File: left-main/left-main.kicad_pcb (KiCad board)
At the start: 2 copper layers, 136 x 123.8 mm, 205 parts, among them P1 CONN_4, P2 CONN_5, P3 CONN_6, P4 CONN_18, Q1 PNP, Q2 PNP, SW11 SPST, SW12 SPST, SW13 SPST, SW14 SPST, SW15 SPST, SW16 SPST, SW17 SPST, SW21 SPST, SW22 SPST, SW23 SPST, SW24 SPST, SW25 SPST, SW27 SPST, SW31 SPST, SW32 SPST, SW33 SPST, SW34 SPST, SW35 SPST, SW37 SPST, SW411 SPST, SW412 SPST, SW42 SPST, SW43 SPST, SW44 SPST, SW45 SPST, SW46 SPST, SW47 SPST, SW51 SPST, SW52 SPST, SW53 SPST, SW54 SPST, SW55 SPST, SW56 SPST, U1 ATMEGA88-A, U2 PCA9634, U3 TPIC6C595, X1 16Mhz

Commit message: Switch 15
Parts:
- SW15: footprint UGL:Cherry_MX -> ugl:Cherry-MX-Matias-Hybrid
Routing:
- net /KEYS_ROW1: track 165.8 -> 166.5 mm
- net Net-(D15-Pad2): track 18.7 -> 17.9 mm
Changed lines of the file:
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@@
 (kicad_pcb (version 4) (host pcbnew 4.0.1-stable)
   (general
-    (links 366)
+    (links 368)
     (no_connects 0)
-    (area 29.35 17.5462 270.000001 165.000001)
+    (area 125.815009 33.896633 261.825015 157.725219)
     (thickness 1.6)
     (drawings 431)
-    (tracks 1379)
+    (tracks 1386)
     (zones 0)
     (modules 205)
@@
   (layers
     (0 F.Cu signal)
-    (31 B.Cu signal)
+    (31 B.Cu signal hide)
     (32 B.Adhes user hide)
     (33 F.Adhes user hide)
@@
   )
   (module UGL:Cherry_MX locked (layer F.Cu)
-    (at 212.820002 65.320214 180)
-    (fp_text reference SW15 (at 0 4.9 180) (layer F.SilkS)
-      (effects (font (size 1.5 1.5) (thickness 0.3)))
-    )
-    (fp_text value SPST (at 0 0 180) (layer F.SilkS) hide
-      (effects (font (size 1.5 1.5) (thickness 0.3)))
-    )
-    (fp_line (start -7.6 -7.6) (end -7.6 7.6) (layer B.SilkS) (width 0.15))
-    (fp_line (start -7.6 7.6) (end 7.6 7.6) (layer B.SilkS) (width 0.15))
-    (fp_line (start 7.6 -7.6) (end 7.6 7.6) (layer B.SilkS) (width 0.15))
-    (fp_line (start -7.6 -7.6) (end 7.6 -7.6) (layer B.SilkS) (width 0.15))
-    (fp_line (start -7.62 -7.62) (end 7.62 -7.62) (layer F.SilkS) (width 0.15))
-    (fp_line (start 7.62 -7.62) (end 7.62 7.62) (layer F.SilkS) (width 0.15))
-    (fp_line (start 7.62 7.62) (end -7.62 7.62) (layer F.SilkS) (width 0.15))
-    (fp_line (start -7.62 7.62) (end -7.62 -7.62) (layer F.SilkS) (width 0.15))
-    (pad "" np_thru_hole circle (at 0 0 180) (size 4 4) (drill 4) (layers *.Cu *.Mask F.SilkS))
-    (pad 2 thru_hole circle (at -3.81 -2.54 180) (size 2.5 2.5) (drill 1.5) (layers *.Cu *.Mask F.SilkS)
-      (net 54 "Net-(D15-Pad2)"))
-    (pad 1 thru_hole circle (at 2.54 -5.08 180) (size 2.5 2.5) (drill 1.5) (layers *.Cu *.Mask F.SilkS)
-      (net 9 /KEYS_ROW1))
-  )
-  (module UGL:Cherry_MX locked (layer F.Cu)
     (at 143.57001 103.320221 180)
     (fp_text reference SW31 (at 0 4.9 180) (layer F.SilkS)
@@
     )
   )
+  (module ugl:Cherry-MX-Matias-Hybrid locked (layer F.Cu)
+    (at 212.820002 65.320214 180)
+    (tags switch)
+    (fp_text reference SW15 (at 0 3.81 180) (layer F.SilkS)
+      (effects (font (thickness 0.3048)))
+    )
+    (fp_text value SPST (at 0 0 180) (layer F.SilkS) hide
+      (effects (font (thickness 0.3048)))
+    )
+    (fp_line (start -7.62 7.62) (end -7.62 -7.62) (layer B.SilkS) (width 0.15))
+    (fp_line (start 7.62 7.62) (end -7.62 7.62) (layer B.SilkS) (width 0.15))
+    (fp_line (start 7.62 -7.62) (end 7.62 7.62) (layer B.SilkS) (width 0.15))
+    (fp_line (start -7.62 -7.62) (end 7.62 -7.62) (layer B.SilkS) (width 0.15))
+    (fp_line (start -7.75 -6.4) (end -7.75 6.4) (layer F.SilkS) (width 0.15))
+    (fp_line (start 7.75 -6.4) (end 7.75 6.4) (layer F.SilkS) (width 0.15))
+    (fp_line (start -7.75 6.4) (end 7.75 6.4) (layer F.SilkS) (width 0.15))
+    (fp_line (start -7.75 -6.4) (end 7.75 -6.4) (layer F.SilkS) (width 0.15))
+    (fp_line (start -7.62 -7.62) (end 7.62 -7.62) (layer F.SilkS) (width 0.15))
+    (fp_line (start 7.62 -7.62) (end 7.62 7.62) (layer F.SilkS) (width 0.15))
+    (fp_line (start 7.62 7.62) (end -7.62 7.62) (layer F.SilkS) (width 0.15))
+    (fp_line (start -7.62 7.62) (end -7.62 -7.62) (layer F.SilkS) (width 0.15))
+    (pad 0 thru_hole circle (at 0 0 180) (size 3.98018 3.98018) (drill 3.98018) (layers *.Cu *.Mask F.SilkS))
+    (pad 1 thru_hole circle (at 2.54 -5.08 180) (size 2.6 2.6) (drill 1.5011) (layers *.Cu *.Mask F.SilkS)
+      (net 9 /KEYS_ROW1))
+    (pad 2 thru_hole circle (at -3.81 -2.54 180) (size 2.6 2.6) (drill 1.5011) (layers *.Cu *.Mask F.SilkS)
+      (net 54 "Net-(D15-Pad2)"))
+    (pad "" thru_hole circle (at -5.08 0 180) (size 1.69926 1.69926) (drill 1.69926) (layers *.Cu *.Mask F.SilkS))
+    (pad "" thru_hole circle (at 5.08 0 180) (size 1.69926 1.69926) (drill 1.69926) (layers *.Cu *.Mask F.SilkS))
+    (pad 1 thru_hole circle (at 2.5 -4.5 180) (size 2.5 2.5) (drill 1.5) (layers *.Cu *.Mask F.SilkS)
+      (net 9 /KEYS_ROW1))
+    (pad 2 thru_hole circle (at -2.5 -4 180) (size 2.5 2.5) (drill 1.5) (layers *.Cu *.Mask F.SilkS)
+      (net 54 "Net-(D15-Pad2)"))
+    (model cherry_mx1.wrl
+      (at (xyz 0 0 0))
+      (scale (xyz 1 1 1))
+      (rotate (xyz 0 0 0))
+    )
+  )
   (gr_line (start 173.482 68.707) (end 170.561 68.707) (angle 90) (layer B.SilkS) (width 0.2))
   (gr_line (start 158.369 69.723) (end 161.036 69.723) (angle 90) (layer B.SilkS) (width 0.2))
@@
   (segment (start 238.5563 60.896) (end 241.3 63.6397) (width 0.4064) (layer B.Cu) (net 8))
   (segment (start 233.3937 112.796) (end 231.6937 114.496) (width 0.4064) (layer B.Cu) (net 8))
+  (segment (start 229.320002 69.820214) (end 230.570001 71.070213) (width 0.4064) (layer F.Cu) (net 9))
+  (segment (start 230.570001 71.070213) (end 245.771526 71.070213) (width 0.4064) (layer F.Cu) (net 9))
+  (segment (start 245.771526 71.070213) (end 246.441525 70.400214) (width 0.4064) (layer F.Cu) (net 9))
+  (segment (start 246.441525 70.400214) (end 248.280002 70.400214) (width 0.4064) (layer F.Cu) (net 9))
+  (segment (start 210.280002 70.400214) (end 211.580001 71.700213) (width 0.4064) (layer F.Cu) (net 9))
+  (segment (start 211.580001 71.700213) (end 227.980003 71.700213) (width 0.4064) (layer F.Cu) (net 9))
+  (segment (start 227.980003 71.700213) (end 229.280002 70.400214) (width 0.4064) (layer F.Cu) (net 9))
   (segment (start 210.280002 70.400214) (end 208.512236 70.400214) (width 0.4064) (layer F.Cu) (net 9))
   (segment (start 208.512236 70.400214) (end 207.212237 71.700213) (width 0.4064) (layer F.Cu) (net 9))
@@
   (segment (start 188.935835 70.976615) (end 189.512236 70.400214) (width 0.4064) (layer F.Cu) (net 9))
   (segment (start 189.512236 70.400214) (end 191.280002 70.400214) (width 0.4064) (layer F.Cu) (net 9))
-  (segment (start 229.320002 69.820214) (end 230.570001 71.070213) (width 0.4064) (layer F.Cu) (net 9))
-  (segment (start 247.070003 71.070213) (end 248.320002 69.820214) (width 0.4064) (layer F.Cu) (net 9))
-  (segment (start 230.570001 71.070213) (end 247.070003 71.070213) (width 0.4064) (layer F.Cu) (net 9))
   (segment (start 153.32001 69.820214) (end 155.087776 69.820214) (width 0.4064) (layer F.Cu) (net 9))
   (segment (start 155.087776 69.820214) (end 156.244177 70.976615) (width 0.4064) (layer F.Cu) (net 9))
@@
   (segment (start 148.657 109.5766) (end 148.757 109.6766) (width 0.4064) (layer B.Cu) (net 9))
   (segment (start 153.207 70.473224) (end 153.28001 70.400214) (width 0.4064) (layer B.Cu) (net 9))
-  (segment (start 229.280002 70.400214) (end 210.280002 70.400214) (width 0.4064) (layer F.Cu) (net 9))
   (segment (start 137.357 73.477204) (end 134.28001 70.400214) (width 0.4064) (layer B.Cu) (net 9))
   (segment (start 137.357 74.796) (end 137.357 73.477204) (width 0.4064) (layer B.Cu) (net 9))
@@
   (segment (start 154.657 110.096) (end 154.657 129.54086) (width 0.4064) (layer F.Cu) (net 39))
   (segment (start 154.657 129.54086) (end 156.912141 131.796001) (width 0.4064) (layer F.Cu) (net 39))
+  (segment (start 212.307 59.346) (end 211.855289 59.346) (width 0.4064) (layer B.Cu) (net 40))
+  (segment (start 206.357 66.213501) (end 206.357 66.896) (width 0.4064) (layer B.Cu) (net 40))
+  (segment (start 211.855289 59.346) (end 206.357 64.844289) (width 0.4064) (layer B.Cu) (net 40))
+  (segment (start 206.357 64.844289) (end 206.357 66.213501) (width 0.4064) (layer B.Cu) (net 40))
+  (segment (start 212.307 54.296) (end 212.307 59.346) (width 0.4064) (layer B.Cu) (net 40))
   (segment (start 194.367454 61.225954) (end 196.664669 61.225954) (width 0.4064) (layer B.Cu) (net 40))
   (segment (start 191.423511 64.169897) (end 194.367454 61.225954) (width 0.4064) (layer B.Cu) (net 40))
@@
   (segment (start 235.770459 142.65708) (end 237.886015 144.772636) (width 0.4064) (layer B.Cu) (net 40))
   (segment (start 237.886015 145.037704) (end 240.07893 147.230619) (width 0.4064) (layer B.Cu) (net 40))
-  (segment (start 212.307 54.296) (end 212.307 60.946) (width 0.4064) (layer B.Cu) (net 40))
   (via (at 206.357 66.896) (size 0.9652) (drill 0.5588) (layers F.Cu B.Cu) (net 40))
   (segment (start 206.357 66.896) (end 203.957 66.896) (width 0.4064) (layer F.Cu) (net 40))
   (via (at 203.957 66.896) (size 0.9652) (drill 0.5588) (layers F.Cu B.Cu) (net 40))
-  (segment (start 212.307 60.946) (end 206.357 66.896) (width 0.4064) (layer B.Cu) (net 40))
   (segment (start 162.397347 98.831437) (end 173.349035 98.831437) (width 0.4064) (layer B.Cu) (net 40))
   (segment (start 173.349035 98.831437) (end 178.587395 93.593077) (width 0.4064) (layer B.Cu) (net 40))
@@
   (segment (start 197.630002 68.859698) (end 191.6937 74.796) (width 0.4064) (layer B.Cu) (net 53))
   (segment (start 197.630002 67.860214) (end 197.630002 68.859698) (width 0.4064) (layer B.Cu) (net 53))
-  (segment (start 201.5937 73.4593) (end 201.5937 74.796) (width 0.4064) (layer B.Cu) (net 54))
-  (segment (start 206.557 68.496) (end 201.5937 73.4593) (width 0.4064) (layer B.Cu) (net 54))
-  (segment (start 215.994216 68.496) (end 206.557 68.496) (width 0.4064) (layer B.Cu) (net 54))
+  (segment (start 201.5937 74.796) (end 202.5823 74.796) (width 0.4064) (layer B.Cu) (net 54))
+  (segment (start 214.070003 68.070215) (end 215.320002 69.320214) (width 0.4064) (layer B.Cu) (net 54))
+  (segment (start 202.5823 74.796) (end 209.308085 68.070215) (width 0.4064) (layer B.Cu) (net 54))
+  (segment (start 209.308085 68.070215) (end 214.070003 68.070215) (width 0.4064) (layer B.Cu) (net 54))
   (segment (start 216.630002 67.860214) (end 215.994216 68.496) (width 0.4064) (layer B.Cu) (net 54))
   (segment (start 235.630002 67.860214) (end 235.630002 68.010214) (width 0.4064) (layer B.Cu) (net 55))

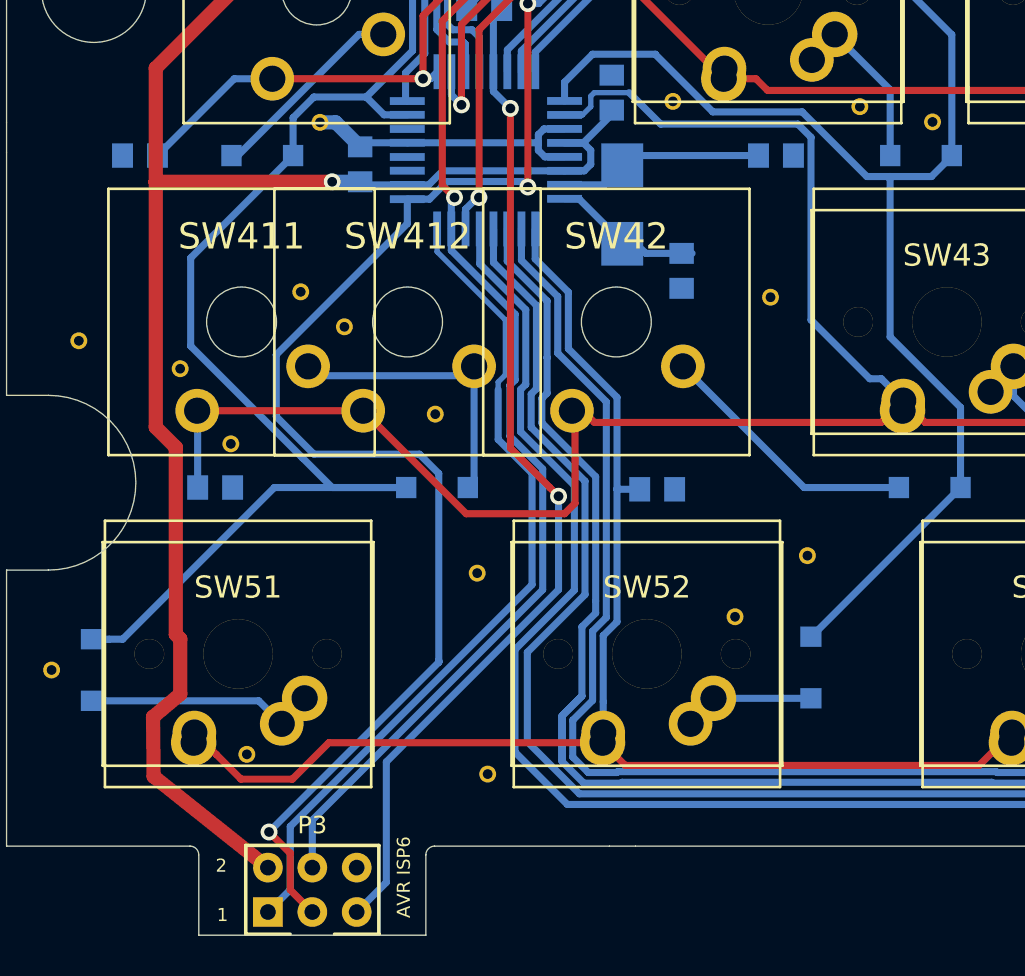
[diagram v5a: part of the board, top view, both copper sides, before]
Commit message: Changes iso keys to matias / cherry mx with holes
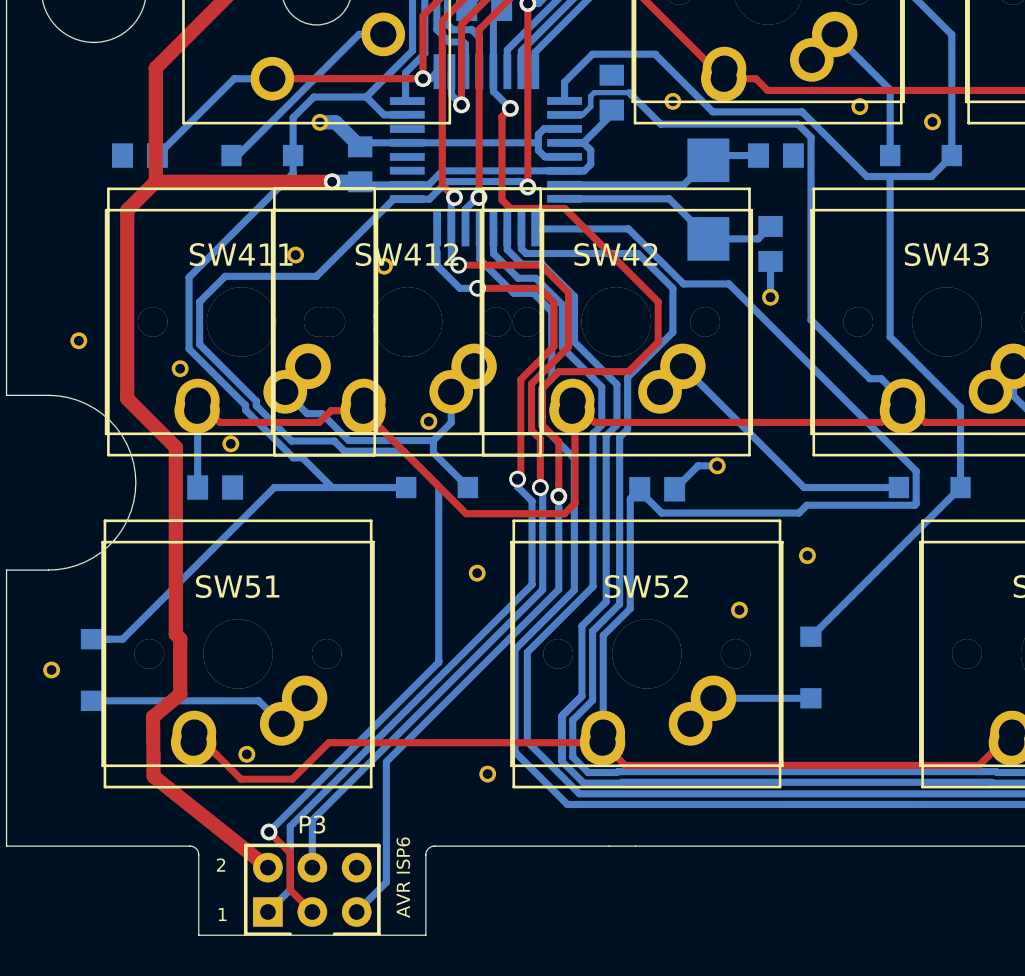
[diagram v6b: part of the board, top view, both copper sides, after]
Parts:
- added via 38/22mil: VAL**, ugl:via_38_22mil, F.Cu at (166.5, 130.6)
- SW411, SW412: footprint UGL:Cherry_MX -> ugl:Cherry-MX-Matias-Hybrid
- SW42: footprint ugl:Cherry_MX -> ugl:Cherry-MX-Matias-Hybrid
- moved C2 5.32 mm to (169.5, 117.9)
- moved X1 4.94 mm to (166.0, 115.3)
- moved via 35/25mil 4.16 mm to (147.4, 119.1)
- moved via 38/22mil 2.12 mm to (142.4, 118.5)
- moved via 35/25mil 0.56 mm to (150.0, 128.0)
- moved via 38/22mil 0.46 mm to (167.8, 138.8)
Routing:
- net /KEYS_ROW5: track 157.3 -> 185.6 mm
- net /RESET: track 58.2 -> 68.3 mm
- net /SCK: track 150.3 -> 157.2 mm
- net /KEYS_COL3: track 160.0 -> 166.9 mm
- net /XTAL2: track 7.47 -> 13.9 mm
- net Net-(D41-Pad2): track 17.0 -> 22.4 mm
- net GND: track 79.1 -> 84.2 mm
- net /MOSI: track 135.5 -> 139.8 mm, vias 2 -> 4
- net /MISO: track 48.1 -> 52.2 mm, vias 0 -> 2
- net Net-(D42-Pad2): track 15.4 -> 17.2 mm
- net /KEYS_COL4: track 205.4 -> 206.9 mm
- net VCC: track 394.0 -> 395.4 mm
- net /RX2: track 135.2 -> 136.4 mm
- net /KEYS_COL5: track 270.0 -> 270.9 mm
- net /KEYS_ROW4: track 168.6 -> 169.4 mm

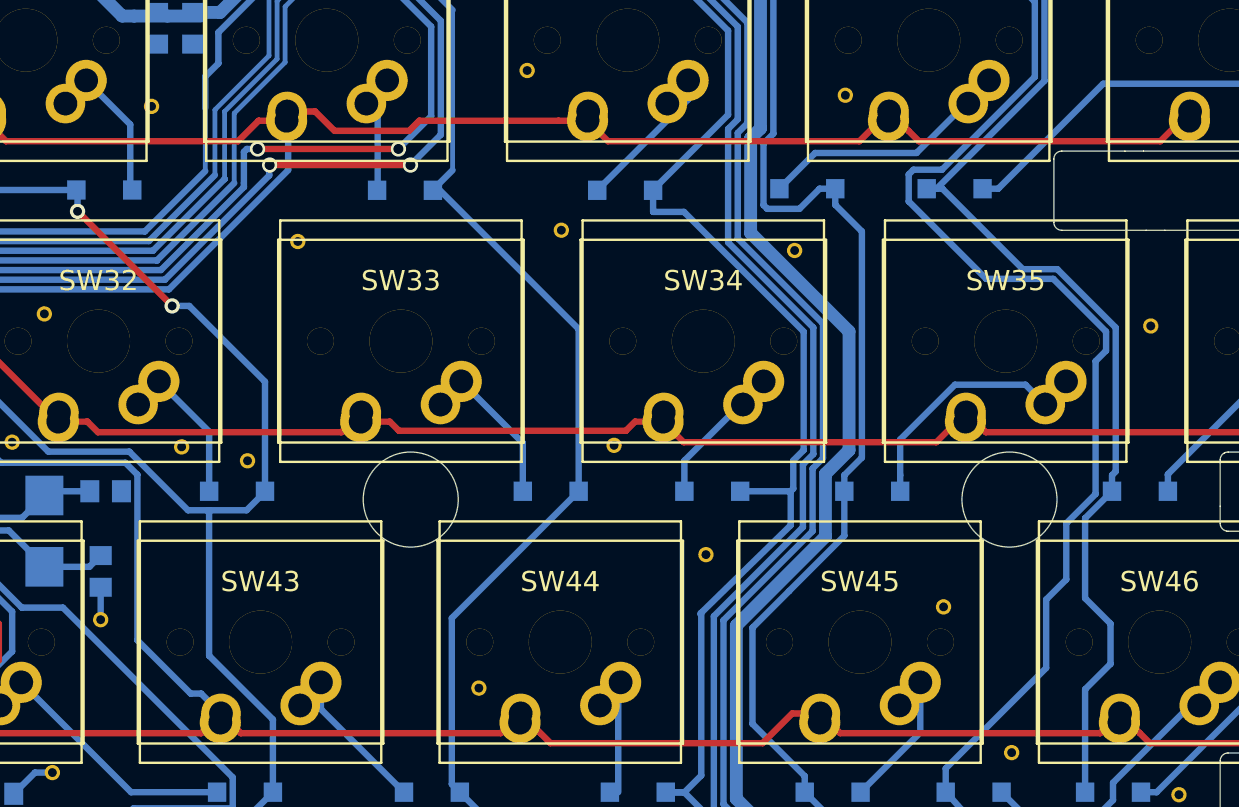
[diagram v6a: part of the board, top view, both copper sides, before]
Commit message: Adds more fill holes
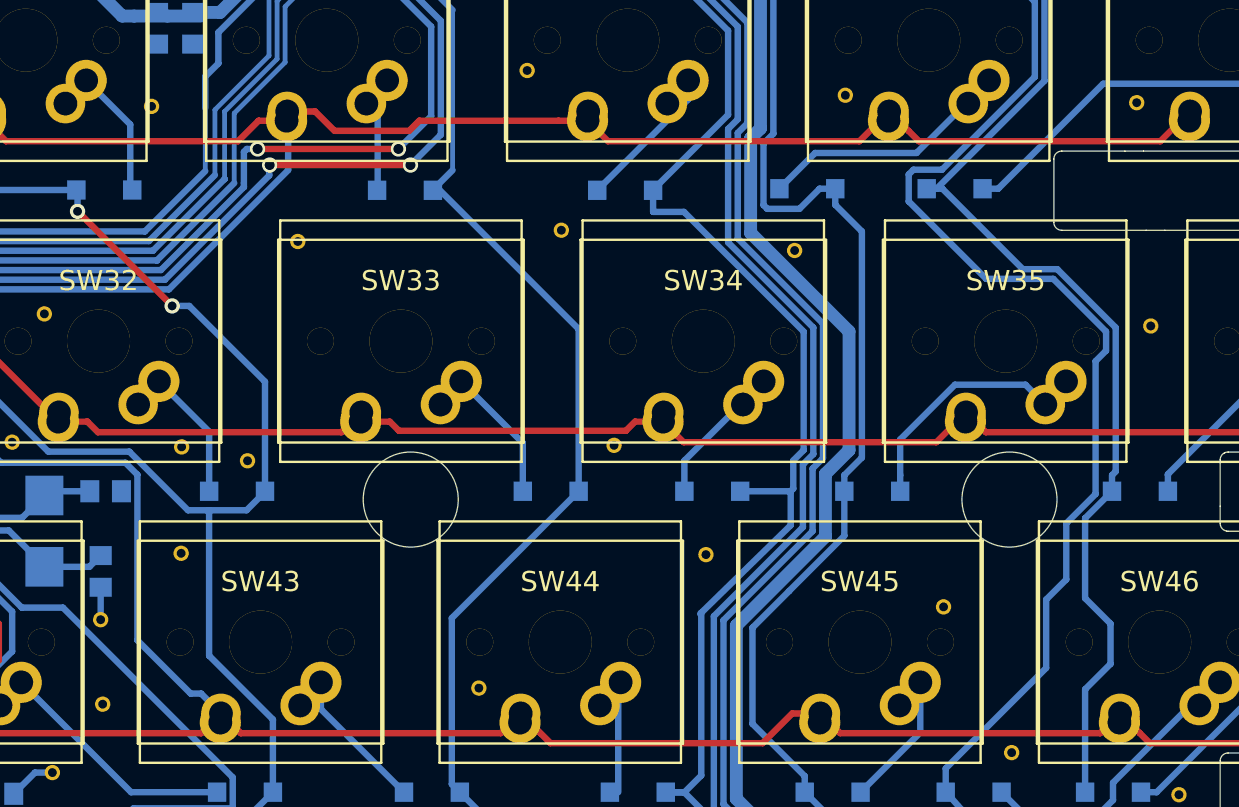
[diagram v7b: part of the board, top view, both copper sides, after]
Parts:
- added via 38/22mil: VAL**, ugl:via_38_22mil, F.Cu at (234.9, 88.3)
- added via 38/22mil: VAL**, ugl:via_38_22mil, F.Cu at (169.7, 126.2)
- added via 38/22mil: VAL**, ugl:via_38_22mil, F.Cu at (174.6, 116.7)
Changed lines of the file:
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@@
 (kicad_pcb (version 4) (host pcbnew 4.0.1-stable)
   (general
-    (links 375)
+    (links 378)
     (no_connects 0)
-    (area 125.815009 33.896633 261.825015 157.725219)
+    (area 29.35 17.5462 270.000001 165.000001)
     (thickness 1.6)
     (drawings 431)
     (tracks 1447)
     (zones 0)
-    (modules 206)
+    (modules 209)
     (nets 97)
   )
@@
     (fp_text reference "via 38/22mil" (at 0 -1.8) (layer F.SilkS) hide
       (effects (font (size 0.75 0.75) (thickness 0.15)))
+    )
+    (fp_text value VAL** (at 0 1.9) (layer F.SilkS) hide
+      (effects (font (size 0.75 0.75) (thickness 0.15)))
+    )
+    (pad "" thru_hole circle (at 0 0) (size 0.9652 0.9652) (drill 0.5588) (layers *.Cu *.Mask F.SilkS)
+      (net 48 GND) (solder_mask_margin -1))
+  )
+  (module ugl:via_38_22mil (layer F.Cu)
+    (at 234.95 88.265)
+    (fp_text reference "via 38/22mil" (at 0 -1.8) (layer F.SilkS) hide
+      (effects (font (size 0.75 0.75) (thickness 0.15)))
+    )
+    (fp_text value VAL** (at 0 1.9) (layer F.SilkS) hide
+      (effects (font (size 0.75 0.75) (thickness 0.15)))
+    )
+    (pad "" thru_hole circle (at 0 0) (size 0.9652 0.9652) (drill 0.5588) (layers *.Cu *.Mask F.SilkS)
+      (net 48 GND) (solder_mask_margin -1))
+  )
+  (module ugl:via_38_22mil (layer F.Cu)
+    (at 169.672 126.238)
+    (fp_text reference "via 38/22mil" (at 0 -1.8) (layer F.SilkS) hide
+      (effects (font (size 0.75 0.75) (thickness 0.15)))
+    )
+    (fp_text value VAL** (at 0 1.9) (layer F.SilkS) hide
+      (effects (font (size 0.75 0.75) (thickness 0.15)))
+    )
+    (pad "" thru_hole circle (at 0 0) (size 0.9652 0.9652) (drill 0.5588) (layers *.Cu *.Mask F.SilkS)
+      (net 48 GND) (solder_mask_margin -1))
+  )
+  (module ugl:via_38_22mil (layer F.Cu)
+    (at 174.625 116.713)
+    (fp_text reference "via 38/22mil" (at 0 -1.8) (layer F.SilkS) hide
+      (effects (font (size 0.75 0.75) (thickness 0.15)))
